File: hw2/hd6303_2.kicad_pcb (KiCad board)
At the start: 2 copper layers, 25 parts, among them J1 Conn_02x20_Odd_Even, J2 Conn_02x06_Odd_Even, J3 Screw_Terminal_01x02, SW1 SW_Push, U2 MAX708, U3 27C512, U4 HD6303RP, U5 HM62256BLP-7, U6 GAL16V8, Y1 4.9152M

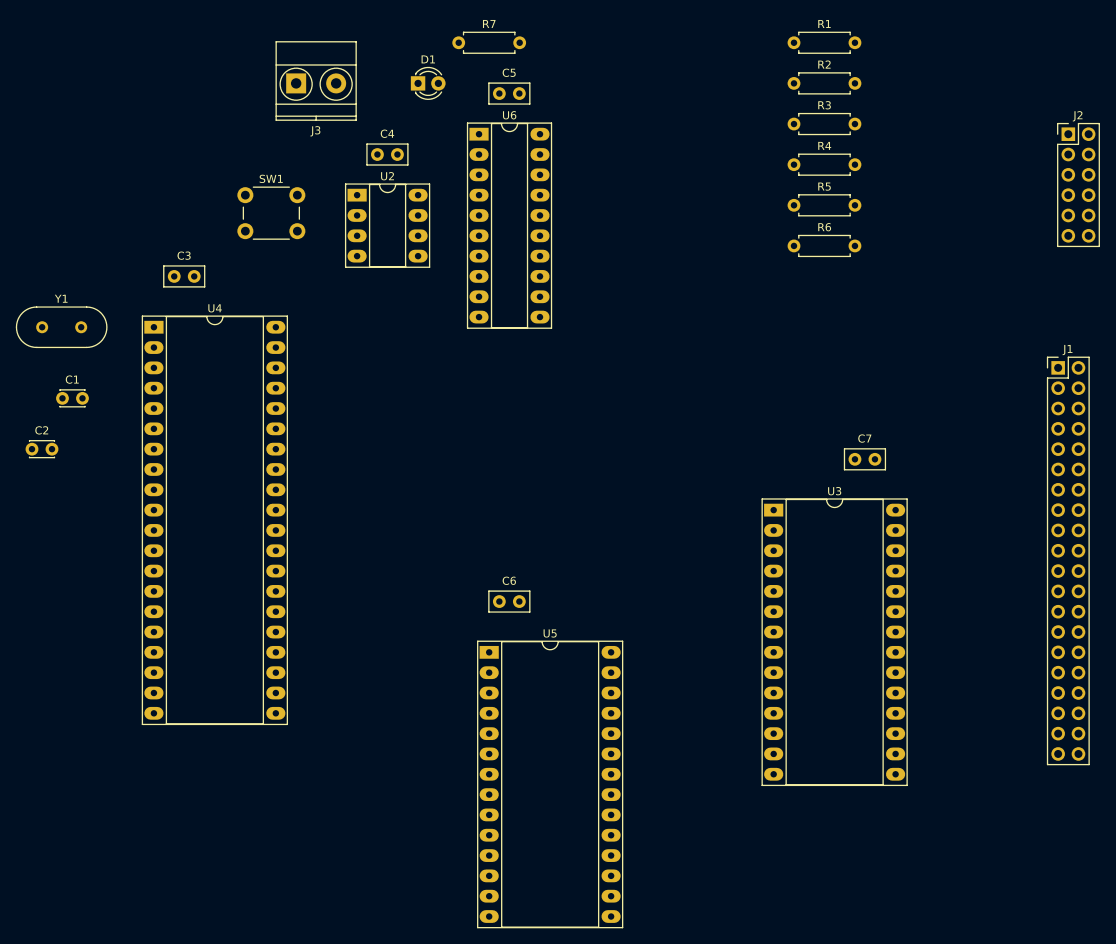
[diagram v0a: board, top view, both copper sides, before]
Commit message: use smaller footprint for resistors
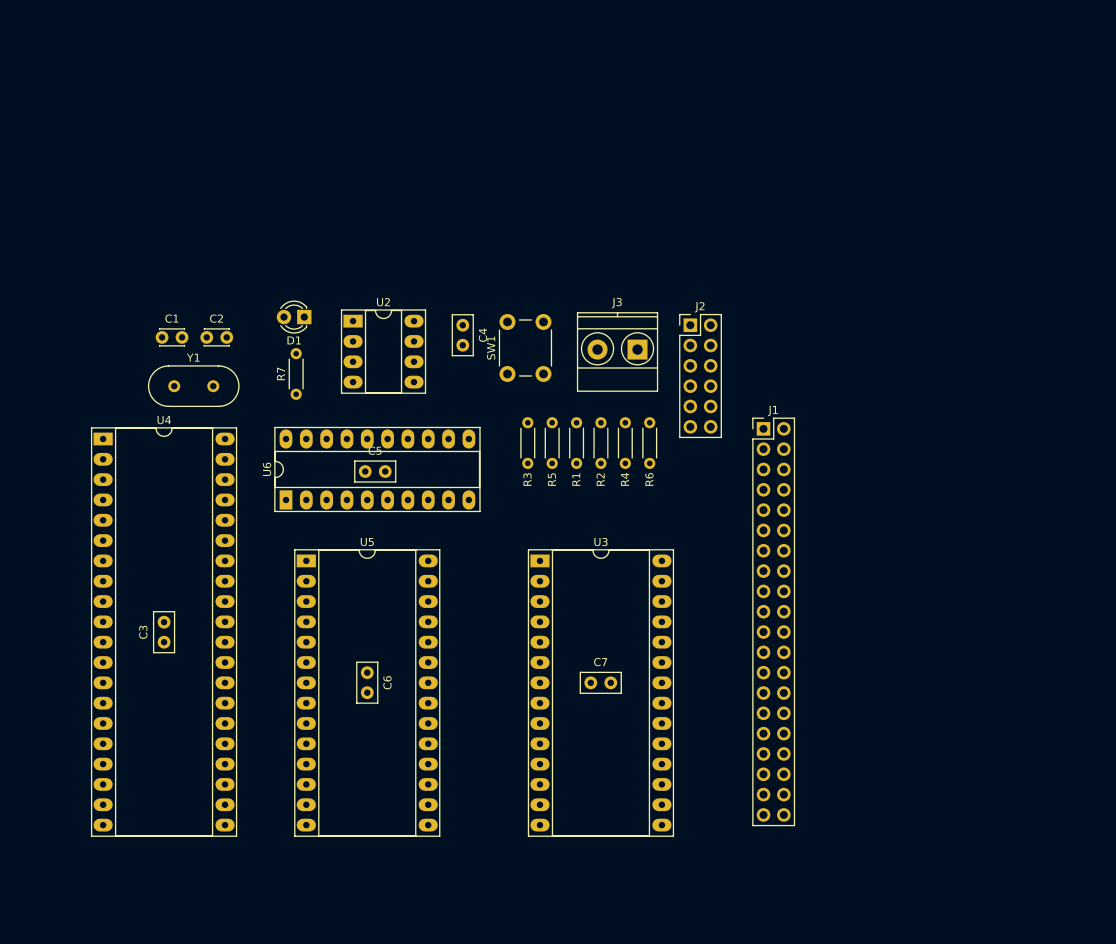
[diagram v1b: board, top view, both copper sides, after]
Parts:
- R1, R2, R3, R4, R5, R6, R7: footprint Resistors_THT:R_Axial_DIN0207_L6.3mm_D2.5mm_P7.62mm_Horizontal -> Resistors_THT:R_Axial_DIN0204_L3.6mm_D1.6mm_P5.08mm_Horizontal
- moved R1 59.2 mm to (139.2, 107.2), turned to 90 degrees
- moved J3 54.1 mm to (146.8, 93.0), turned to 180 degrees
- moved R2 53.3 mm to (142.2, 107.2), turned to 90 degrees
- moved J2 52.9 mm to (153.4, 89.9)
- moved U6 51.7 mm to (102.9, 111.8), turned to 90 degrees
- moved C5 50.1 mm to (112.8, 108.2)
- moved R3 50.0 mm to (133.1, 102.1), turned to 270 degrees
- moved R7 48.4 mm to (104.1, 98.6), turned to 90 degrees
- moved C3 45.7 mm to (87.6, 129.5), turned to 90 degrees
- moved C7 43.3 mm to (141.0, 134.6)
- moved R4 42.9 mm to (145.3, 107.2), turned to 90 degrees
- moved R5 40.6 mm to (136.1, 102.1), turned to 270 degrees
- moved SW1 39.7 mm to (130.6, 96.0), turned to 90 degrees
- moved J1 37.6 mm to (162.6, 102.9)
- moved R6 32.6 mm to (148.3, 107.2), turned to 90 degrees
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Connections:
- J1 pad 33: VCC -> /-RES
- U2 pad 7: Net-(U2-Pad7) -> /-RES
- U4 pad 6: Net-(U2-Pad7) -> /-RES

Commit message: reasonable component placement?
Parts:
- added ?: MountingHole_3.2mm_M3_ISO14580, Mounting_Holes:MountingHole_3.2mm_M3_ISO14580, F.Cu at (79.8, 90.4)
- added ?: MountingHole_3.2mm_M3_ISO14580, Mounting_Holes:MountingHole_3.2mm_M3_ISO14580, F.Cu at (164.6, 90.4)
- added ?: MountingHole_3.2mm_M3_ISO14580, Mounting_Holes:MountingHole_3.2mm_M3_ISO14580, F.Cu at (79.8, 154.9)
- added ?: MountingHole_3.2mm_M3_ISO14580, Mounting_Holes:MountingHole_3.2mm_M3_ISO14580, F.Cu at (164.6, 154.9)
- moved C4 14.9 mm to (110.2, 91.9)
- moved R1 6.10 mm to (133.1, 107.2)
- moved J1 3.84 mm to (162.1, 99.1)
- moved U4 3.57 mm to (80.3, 100.6)
- moved U2 3.56 mm to (114.8, 89.4)
- moved Y1 3.25 mm to (86.9, 95.0)
- moved R7 3.21 mm to (105.2, 95.5), turned to 180 degrees
- moved R3 3.05 mm to (136.1, 102.1)
- moved R5 3.05 mm to (139.2, 102.1)
- moved SW1 2.54 mm to (128.0, 96.0)
- moved D1 2.27 mm to (104.1, 90.9)
- moved C2 2.27 mm to (90.9, 90.4)
- moved C1 1.14 mm to (87.9, 90.4), turned to 180 degrees

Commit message: apply OSHPark design rules
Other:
- net class Default: clearance 0.2 -> 0.1524; trace_width 0.25 -> 0.1524; via_dia 0.6 -> 0.6858; via_drill 0.4 -> 0.3302
- rule trace_clearance: 0.2 -> 0.1524
- rule trace_min: 0.2 -> 0.1524
- rule via_min_drill: 0.3 -> 0.3302
- rule via_min_size: 0.4 -> 0.6858
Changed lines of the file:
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@@
     (0 F.Cu signal)
     (31 B.Cu signal)
-    (32 B.Adhes user)
-    (33 F.Adhes user)
-    (34 B.Paste user)
-    (35 F.Paste user)
     (36 B.SilkS user)
     (37 F.SilkS user)
     (38 B.Mask user)
     (39 F.Mask user)
-    (40 Dwgs.User user)
-    (41 Cmts.User user)
-    (42 Eco1.User user)
-    (43 Eco2.User user)
     (44 Edge.Cuts user)
-    (45 Margin user)
-    (46 B.CrtYd user)
-    (47 F.CrtYd user)
-    (48 B.Fab user)
-    (49 F.Fab user)
   )
   (setup
-    (last_trace_width 0.25)
-    (trace_clearance 0.2)
+    (last_trace_width 0.1524)
+    (trace_clearance 0.1524)
     (zone_clearance 0.508)
     (zone_45_only no)
-    (trace_min 0.2)
+    (trace_min 0.1524)
     (segment_width 0.2)
     (edge_width 0.15)
-    (via_size 0.6)
-    (via_drill 0.4)
-    (via_min_size 0.4)
-    (via_min_drill 0.3)
-    (uvia_size 0.3)
-    (uvia_drill 0.1)
+    (via_size 0.6858)
+    (via_drill 0.3302)
+    (via_min_size 0.6858)
+    (via_min_drill 0.3302)
+    (uvia_size 0.6858)
+    (uvia_drill 0.3302)
     (uvias_allowed no)
-    (uvia_min_size 0.2)
-    (uvia_min_drill 0.1)
+    (uvia_min_size 0)
+    (uvia_min_drill 0)
     (pcb_text_width 0.3)
     (pcb_text_size 1.5 1.5)
@@
   (net 59 /-RES)
   (net_class Default "This is the default net class."
-    (clearance 0.2)
-    (trace_width 0.25)
-    (via_dia 0.6)
-    (via_drill 0.4)
-    (uvia_dia 0.3)
-    (uvia_drill 0.1)
+    (clearance 0.1524)
+    (trace_width 0.1524)
+    (via_dia 0.6858)
+    (via_drill 0.3302)
+    (uvia_dia 0.6858)
+    (uvia_drill 0.3302)
     (add_net /-IOEN0)
     (add_net /-IOEN1)

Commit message: started routing some traces
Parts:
- moved C3 3.34 mm to (88.1, 126.2)
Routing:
- net GND: track 0.00 -> 172.4 mm, vias 0 -> 2
- net VCC: track 0.00 -> 96.1 mm, vias 0 -> 2
- net Net-(C2-Pad1): track 0.00 -> 27.7 mm, vias 0 -> 1
- net Net-(C1-Pad1): track 0.00 -> 21.6 mm, vias 0 -> 1
- net Net-(SW1-Pad2): track 0.00 -> 19.1 mm
- net Net-(D1-Pad1): track 0.00 -> 18.9 mm
- net Net-(D1-Pad2): track 0.00 -> 5.20 mm
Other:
- net class Power added: clearance 0.254, trace_width 0.254, via_dia 0.6858, via_drill 0.3302

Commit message: continuing to route traces
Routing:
- net /D3: track 0.00 -> 69.9 mm, vias 0 -> 2
- net /D4: track 0.00 -> 63.4 mm, vias 0 -> 2
- net /D0: track 0.00 -> 56.8 mm, vias 0 -> 2
- net /D1: track 0.00 -> 55.7 mm, vias 0 -> 2
- net /D2: track 0.00 -> 54.7 mm, vias 0 -> 2
- net /D5: track 0.00 -> 52.3 mm, vias 0 -> 1
- net /D6: track 0.00 -> 48.2 mm, vias 0 -> 2
- net /D7: track 0.00 -> 43.2 mm, vias 0 -> 2
- net /A0: track 0.00 -> 36.9 mm, vias 0 -> 2
- net /A1: track 0.00 -> 31.6 mm, vias 0 -> 2
- net /A10: track 0.00 -> 30.5 mm, vias 0 -> 2
- net /A3: track 0.00 -> 29.0 mm, vias 0 -> 2
- net /A2: track 0.00 -> 25.8 mm
- net GND: track 172.4 -> 196.6 mm, vias 2 -> 3
- net VCC: track 96.1 -> 117.7 mm, vias 2 -> 3

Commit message: more traces...
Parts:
- moved C7 1.57 mm to (142.4, 134.0), turned to 270 degrees
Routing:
- net /-RES: track 0.00 -> 150.3 mm, vias 0 -> 5
- net /A7: track 0.00 -> 78.8 mm, vias 0 -> 1
- net GND: track 196.6 -> 271.5 mm, vias 3 -> 6
- net /A6: track 0.00 -> 74.1 mm, vias 0 -> 2
- net /A5: track 0.00 -> 69.3 mm, vias 0 -> 2
- net /A4: track 0.00 -> 64.4 mm, vias 0 -> 2
- net VCC: track 117.7 -> 155.9 mm, vias 3 -> 6
- net /D3: track 69.9 -> 101.3 mm, vias 2 -> 4
- net /A3: track 29.0 -> 59.3 mm
- net /D6: track 48.2 -> 78.5 mm
- net /A0: track 36.9 -> 67.1 mm
- net /D0: track 56.8 -> 87.1 mm
- net /A2: track 25.8 -> 56.1 mm
- net /D7: track 43.2 -> 73.5 mm
- net /D4: track 63.4 -> 93.6 mm
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
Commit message: more traces, getting there...
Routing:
- net /A14: track 0.00 -> 94.4 mm, vias 0 -> 4
- net /A11: track 0.00 -> 86.4 mm, vias 0 -> 3
- net /A13: track 0.00 -> 84.8 mm, vias 0 -> 2
- net /-RMEM: track 0.00 -> 77.1 mm, vias 0 -> 3
- net /-ROMEN: track 0.00 -> 75.5 mm, vias 0 -> 2
- net /A15: track 0.00 -> 62.9 mm, vias 0 -> 3
- net /A10: track 30.5 -> 88.3 mm, vias 2 -> 3
- net /A9: track 0.00 -> 56.1 mm
- net /A8: track 0.00 -> 56.0 mm
- net /-RAMEN: track 0.00 -> 43.3 mm, vias 0 -> 1
- net /A12: track 30.2 -> 67.9 mm, vias 0 -> 3
- net VCC: track 155.9 -> 186.7 mm, vias 6 -> 7
- net GND: track 271.5 -> 290.4 mm
- net /A2: track 56.1 -> 57.1 mm

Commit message: more traces routed...
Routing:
- net /D0: track 87.1 -> 141.3 mm, vias 2 -> 4
- net /D2: track 85.0 -> 138.9 mm, vias 2 -> 4
- net /D1: track 85.9 -> 139.8 mm, vias 2 -> 4
- net /D3: track 101.3 -> 144.1 mm, vias 4 -> 5
- net VCC: track 186.7 -> 228.9 mm, vias 7 -> 8
- net GND: track 290.4 -> 328.1 mm, vias 6 -> 7
- net /D4: track 93.6 -> 130.5 mm, vias 2 -> 3
- net /D5: track 82.5 -> 111.8 mm, vias 1 -> 3
- net /D6: track 78.5 -> 102.7 mm, vias 2 -> 4
- net /D7: track 73.4 -> 92.8 mm, vias 2 -> 4
